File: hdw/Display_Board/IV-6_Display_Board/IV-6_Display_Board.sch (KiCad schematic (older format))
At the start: 0 parts

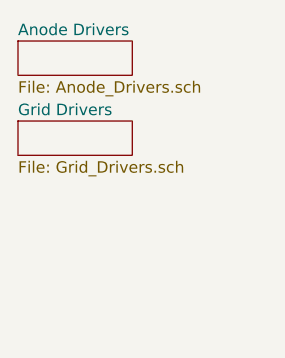
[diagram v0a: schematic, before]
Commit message: Started IV-6 display board, continued logic board development
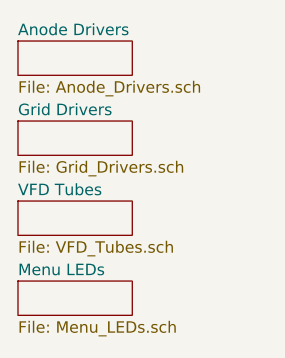
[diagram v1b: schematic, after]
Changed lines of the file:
@@
 EESchema Schematic File Version 4
-EELAYER 29 0
+EELAYER 30 0
 EELAYER END
 $Descr A 11000 8500
 encoding utf-8
-Sheet 1 3
+Sheet 1 5
 Title ""
 Date ""
@@
 F1 "Grid_Drivers.sch" 50
 $EndSheet
+$Sheet
+S 1640 2110 500  150
+U 5E0A3762
+F0 "VFD Tubes" 50
+F1 "VFD_Tubes.sch" 50
+$EndSheet
+$Sheet
+S 1640 2460 500  150
+U 5E0A7959
+F0 "Menu LEDs" 50
+F1 "Menu_LEDs.sch" 50
+$EndSheet
 $EndSCHEMATC

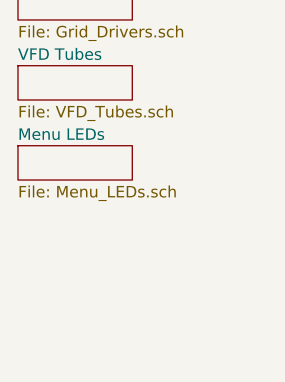
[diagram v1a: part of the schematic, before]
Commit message: Added backup RTC, IO connector, other stuff
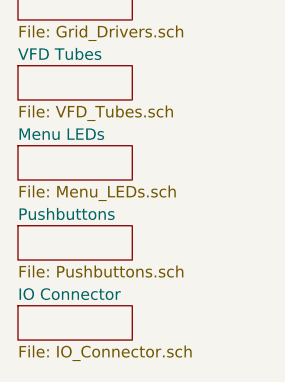
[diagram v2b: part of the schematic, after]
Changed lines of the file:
@@
 EESchema Schematic File Version 4
+LIBS:IV-6_Display_Board-cache
 EELAYER 30 0
 EELAYER END
 $Descr A 11000 8500
 encoding utf-8
-Sheet 1 5
+Sheet 1 7
 Title ""
 Date ""
@@
 F1 "Menu_LEDs.sch" 50
 $EndSheet
+$Sheet
+S 1640 2810 500  150
+U 5E28CFDF
+F0 "Pushbuttons" 50
+F1 "Pushbuttons.sch" 50
+$EndSheet
+$Sheet
+S 1640 3160 500  150
+U 5E2AA002
+F0 "IO Connector" 50
+F1 "IO_Connector.sch" 50
+$EndSheet
 $EndSCHEMATC

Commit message: More IV6 board dev
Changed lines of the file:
@@
 $Descr A 11000 8500
 encoding utf-8
-Sheet 1 7
+Sheet 1 9
 Title ""
 Date ""
@@
 S 1640 2810 500  150
 U 5E28CFDF
-F0 "Pushbuttons" 50
-F1 "Pushbuttons.sch" 50
+F0 "Pushbuttons 1" 50
+F1 "Pushbuttons_1.sch" 50
 $EndSheet
 $Sheet
-S 1640 3160 500  150
+S 1640 3860 500  150
 U 5E2AA002
 F0 "IO Connector" 50
 F1 "IO_Connector.sch" 50
 $EndSheet
+$Sheet
+S 1640 3160 500  150
+U 5E3C97B4
+F0 "Pushbuttons 2" 50
+F1 "Pushbuttons_2.sch" 50
+$EndSheet
+$Sheet
+S 1640 3510 500  150
+U 5E3CBFDA
+F0 "Pushbuttons 3" 50
+F1 "Pushbuttons_3.sch" 50
+$EndSheet
 $EndSCHEMATC

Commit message: Display board tweaks, added buzzer, other stuff
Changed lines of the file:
@@
 $Descr A 11000 8500
 encoding utf-8
-Sheet 1 9
+Sheet 1 12
 Title ""
 Date ""
@@
 F1 "Pushbuttons_3.sch" 50
 $EndSheet
+$Sheet
+S 1640 4210 500  150
+U 5E3D888C
+F0 "Display Telemetry" 50
+F1 "Display_Telemetry.sch" 50
+$EndSheet
+$Sheet
+S 1640 4560 500  150
+U 5E24454D
+F0 "Colons" 50
+F1 "Colons.sch" 50
+$EndSheet
+$Sheet
+S 1640 4910 500  150
+U 5E249DA1
+F0 "Bulk Capacitance" 50
+F1 "Bulk_Capacitance.sch" 50
+$EndSheet
 $EndSCHEMATC

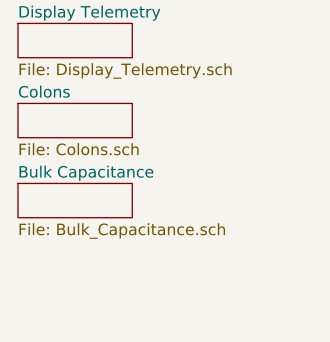
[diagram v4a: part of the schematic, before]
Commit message: Added TOF to display board
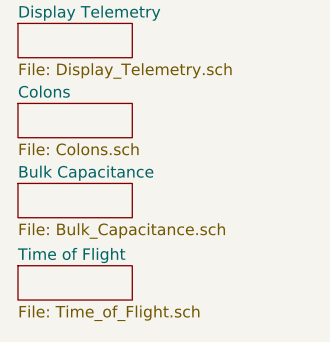
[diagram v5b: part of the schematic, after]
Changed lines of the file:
@@
 $Descr A 11000 8500
 encoding utf-8
-Sheet 1 12
+Sheet 1 13
 Title ""
 Date ""
@@
 F1 "Bulk_Capacitance.sch" 50
 $EndSheet
+$Sheet
+S 1640 5270 500  150
+U 5E2A7EE3
+F0 "Time of Flight" 50
+F1 "Time_of_Flight.sch" 50
+$EndSheet
 $EndSCHEMATC

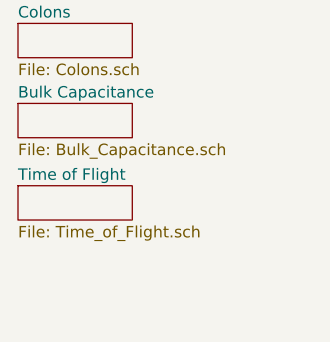
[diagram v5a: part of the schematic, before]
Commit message: Started display board PCB
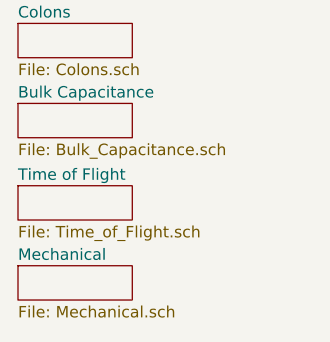
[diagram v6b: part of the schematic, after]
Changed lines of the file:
@@
 $Descr A 11000 8500
 encoding utf-8
-Sheet 1 13
+Sheet 1 14
 Title ""
 Date ""
@@
 F1 "Time_of_Flight.sch" 50
 $EndSheet
+$Sheet
+S 1640 5620 500  150
+U 5E539601
+F0 "Mechanical" 50
+F1 "Mechanical.sch" 50
+$EndSheet
 $EndSCHEMATC
